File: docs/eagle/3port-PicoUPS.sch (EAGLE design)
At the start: 44 parts, among them IC1 MAX471CPA, IC2 MAX471CPA, IC3 MAX471CPA, IC6 7805TV, U1 P012PTH

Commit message: Replaced 7805 with SMD LM1117 - moved it up the board in preparation of adding switches on the output ports
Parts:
- removed IC6: 7805TV, linear:7805TV
- removed R21, R22, R23: 10k, rcl:R-TRIMM3296W
- added IC4: REG1117, burr-brown:REG1117
- added R2, R3, R7: 1k, SparkFun-Passives:RESISTOR0603-RES
- C1: value 100uF -> 10uF; device SparkFun-Capacitors:100UF-25V-20%(PTH) -> SparkFun-Capacitors:10UF-16V-10%(TANT)
- C2: device SparkFun-Capacitors:100UF-25V-20%(PTH) -> SparkFun-Capacitors:10UF-16V-10%(TANT)
- R10, R8, R9: value 1k -> 10k; device SparkFun-Passives:RESISTOR0603-RES -> rcl:R-TRIMM3296W
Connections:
- net 12V: now also IC4.VIN, R8.E; no longer IC6.VI, R21.E
- net 5V: now also IC4.VOUT; no longer IC6.VO
- net BATT-UPS: now also R9.E; no longer R22.E
- net GND: now also IC4.GND, R10.A, R2.2, R3.2, R8.A, R9.A; no longer IC6.GND, R21.A, R22.A, R23.A, R5.2, R6.2
- net I1: now also R2.1; no longer R4.1
- net I2: now also R3.1; no longer R5.1
- net I3: now also R4.1; no longer R6.1
- net N$6: now also R5.2; no longer R8.2
- net N$7: now also R6.2; no longer R9.2
- net N$8: now also R7.2; no longer R10.2
- net OUT1: now also R5.1; no longer R8.1
- net OUT2: now also R6.1; no longer R9.1
- net OUT3: now also R7.1; no longer R10.1
- net V-BATT: now also R9.S; no longer R22.S
- net V-UPS: now also R8.S; no longer R21.S
- net V-VCC: now also R10.S; no longer R23.S
- net VCC-UPS: now also R10.E; no longer R23.E
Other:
- moved on the sheet: C1, C2, R4, R5, R6

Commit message: Upgraded Eagle to 8.2.2; named 'VCC' and 'BATT' signal lines
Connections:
- net N$10 renamed BATT
- net N$9 renamed VCC
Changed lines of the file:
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@@
 <?xml version="1.0" encoding="utf-8"?>
 <!DOCTYPE eagle SYSTEM "eagle.dtd">
-<eagle version="7.6.0">
+<eagle version="8.2.2">
 <drawing>
 <settings>
@@
 </segment>
 </net>
-<net name="N$9" class="0">
+<net name="VCC" class="0">
 <segment>
 <pinref part="VCC-IN" gate="G$1" pin="P"/>
@@
 </segment>
 </net>
-<net name="N$10" class="0">
+<net name="BATT" class="0">
 <segment>
 <pinref part="BATT-IN" gate="G$1" pin="P"/>

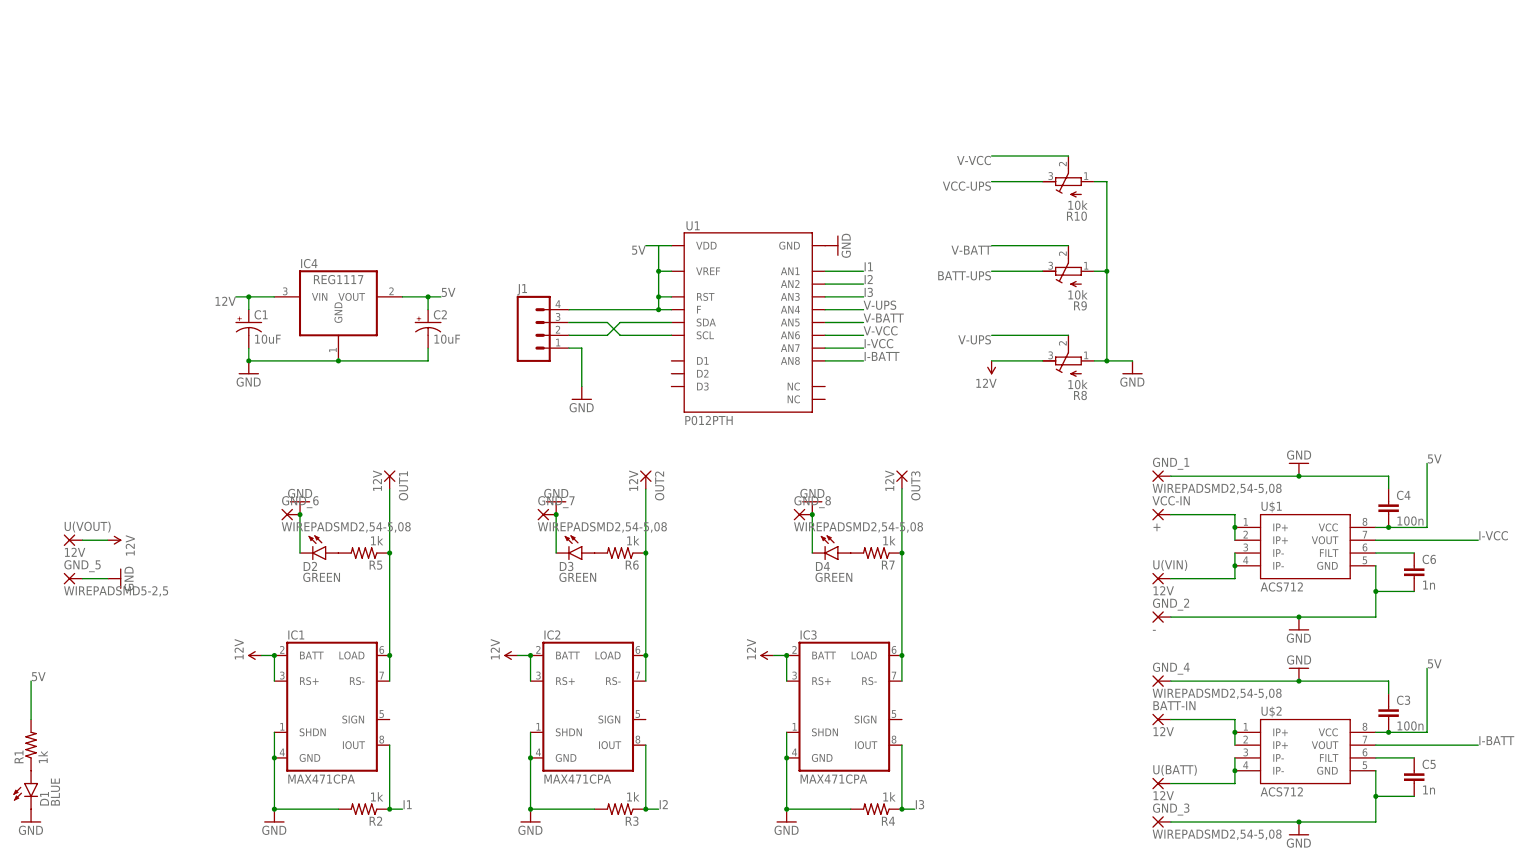
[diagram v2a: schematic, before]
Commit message: Redesign the output section to include the relays and drivers.
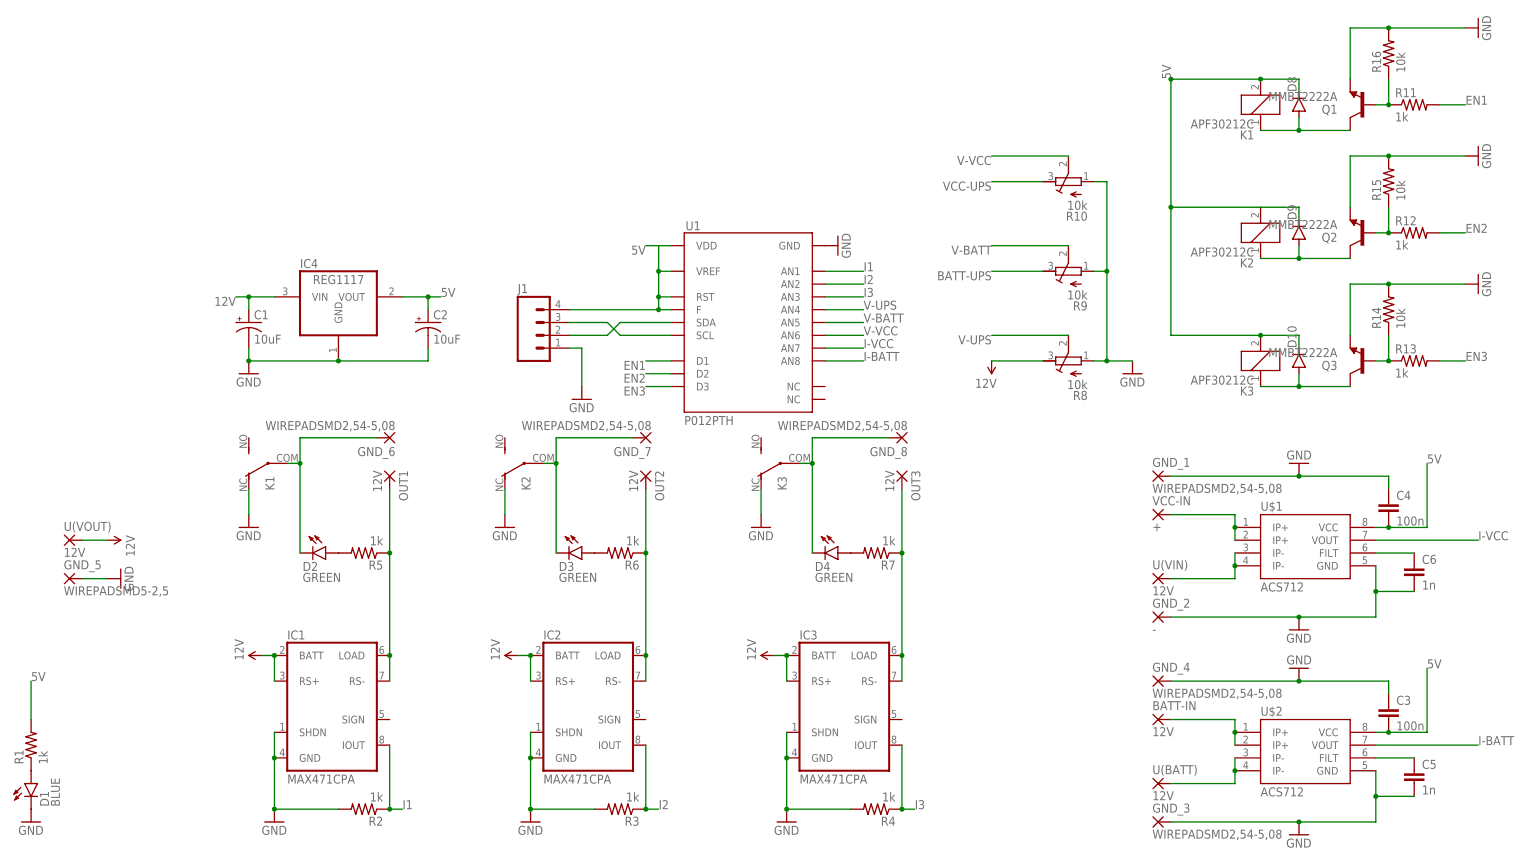
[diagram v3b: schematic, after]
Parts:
- added D10, D8, D9: (no value), SparkFun-DiscreteSemi:DIODESOD123
- added K1, K2, K3: APF30212C, relay:APF30212C
- added Q1, Q2, Q3: MMBT2222A, SparkFun-DiscreteSemi:TRANSISTOR_NPNMMBT2222A
- added R11, R12, R13: 1k, SparkFun-Passives:RESISTOR0805-RES
- added R14, R15, R16: 10k, SparkFun-Passives:RESISTOR0805-RES
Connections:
- new net EN1: R11.2, U1.D1
- new net EN2: R12.2, U1.D2
- new net EN3: R13.2, U1.D3
- new net GND_6: D2.C, GND_6.P, K12.P
- new net GND_7: D3.C, GND_7.P, K22.P
- new net GND_8: D4.C, GND_8.P, K32.P
- new net N$10: D10.A, K31.1, Q3.C
- new net N$11: Q1.B, R11.1, R16.1
- new net N$13: Q2.B, R12.1, R15.1
- new net N$14: Q3.B, R13.1, R14.1
- new net N$5: D8.A, K11.1, Q1.C
- new net N$9: D9.A, K21.1, Q2.C
- net 5V: now also D10.C, D8.C, D9.C, K11.2, K21.2, K31.2
- net GND: now also K12.O, K22.O, K32.O, Q1.E, Q2.E, Q3.E, R14.2, R15.2, R16.2; no longer D2.C, D3.C, D4.C, GND_6.P, GND_7.P, GND_8.P
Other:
- moved on the sheet: GND_6, GND_7, GND_8

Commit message: Move from 0603 to 0805 components
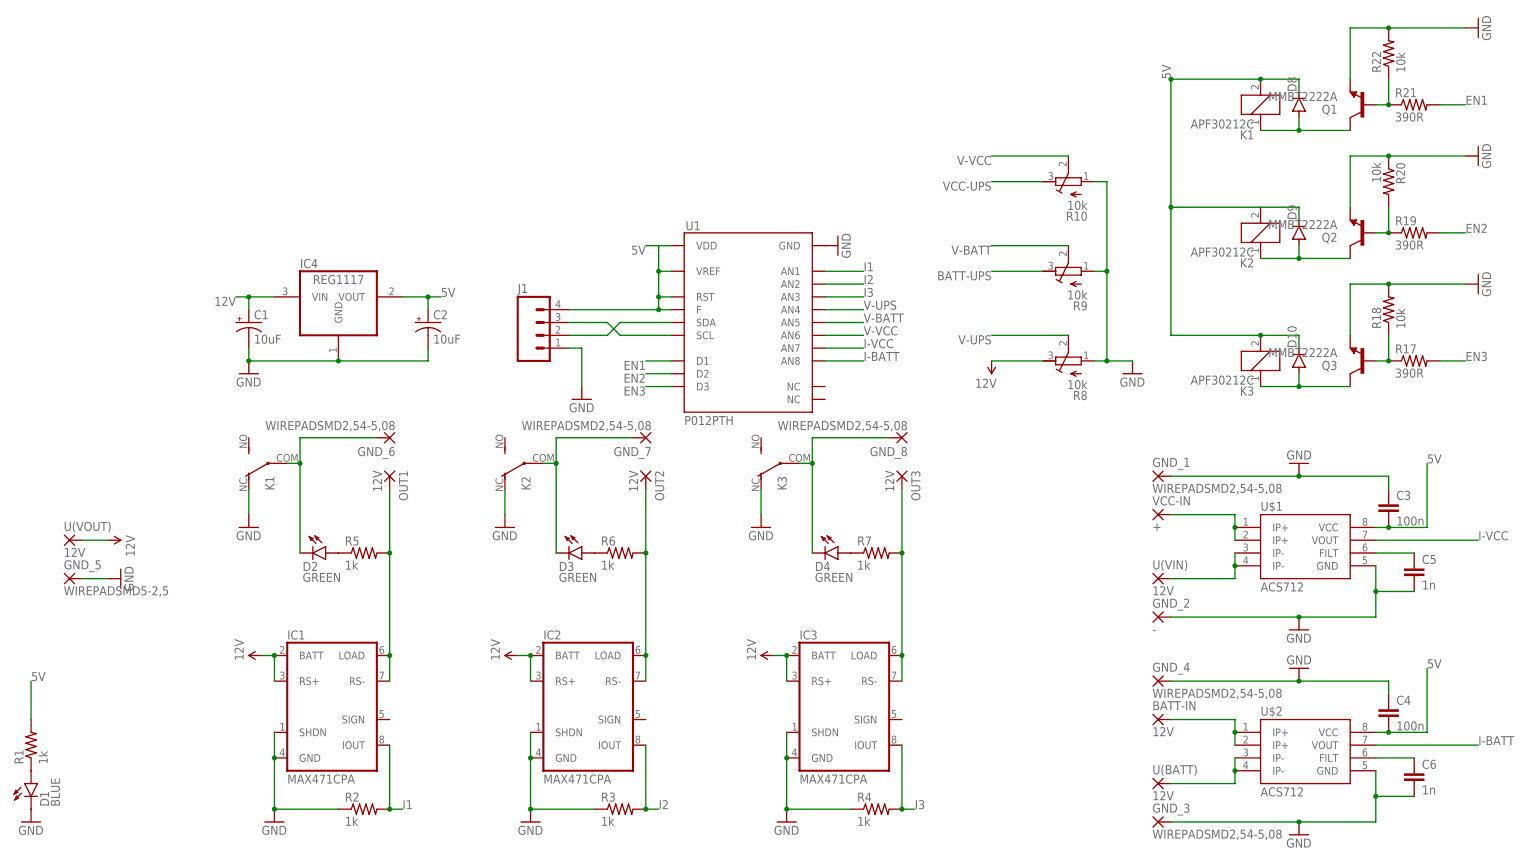
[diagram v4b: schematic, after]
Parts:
- C3, C4, C5, C6: device SparkFun-Capacitors:CAP0603-CAP -> SparkFun-Capacitors:CAP0805
- R1, R2, R3, R4, R5, R6, R7: device SparkFun-Passives:RESISTOR0603-RES -> SparkFun-Passives:RESISTOR0805-RES
- R17, R19, R21: value 1k -> 390R
- renumbered R11 to R21, R12 to R19, R13 to R17, R14 to R18, R15 to R20, R16 to R22
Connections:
- removed net N$6: D2.A, R5.2
- removed net N$7: D3.A, R6.2
- removed net N$8: D4.A, R7.2
- new net N$2: D2.A, R5.1
- new net N$3: D3.A, R6.1
- new net N$4: D4.A, R7.1
- net GND: now also R2.1, R20.1, R3.1, R4.1; no longer R2.2, R20.2, R3.2, R4.2
- net I1: now also R2.2; no longer R2.1
- net I2: now also R3.2; no longer R3.1
- net I3: now also R4.2; no longer R4.1
- net N$12: now also C5.1; no longer C6.1
- net N$13: now also R20.2; no longer R20.1
- net N$15: now also C6.1; no longer C5.1
- net OUT1: now also R5.2; no longer R5.1
- net OUT2: now also R6.2; no longer R6.1
- net OUT3: now also R7.2; no longer R7.1
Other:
- moved on the sheet: C3, C4, C5, C6, R2, R3, R4, R5, R6, R7

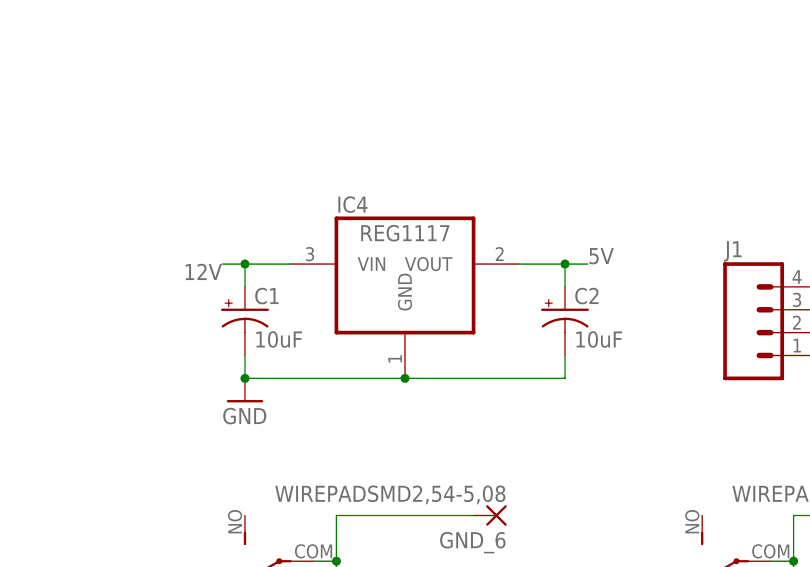
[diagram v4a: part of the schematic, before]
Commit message: Swap out AMS1117 for LM7805, as the former has max voltage of 15V, while we're running at 18V - LM7805 is rated to 20V
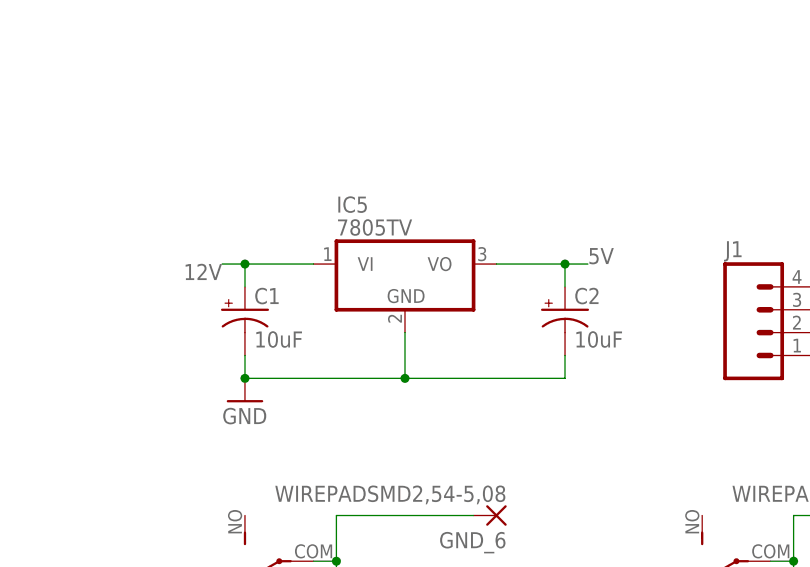
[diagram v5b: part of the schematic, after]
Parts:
- removed IC4: REG1117, burr-brown:REG1117
- added IC5: 7805TV, linear:7805TV
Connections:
- net 12V: now also IC5.VI; no longer IC4.VIN
- net 5V: now also IC5.VO; no longer IC4.VOUT
- net GND: now also IC5.GND; no longer IC4.GND
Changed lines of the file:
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@@
 <part name="J1" library="SparkFun-Connectors" deviceset="M04" device="PTH"/>
 <part name="GND16" library="SparkFun-Aesthetics" deviceset="GND" device=""/>
-<part name="IC4" library="burr-brown" deviceset="REG1117" device=""/>
 <part name="C1" library="SparkFun-Capacitors" deviceset="10UF-16V-10%(TANT)" device="" value="10uF"/>
 <part name="C2" library="SparkFun-Capacitors" deviceset="10UF-16V-10%(TANT)" device="" value="10uF"/>
@@
 <part name="C4" library="SparkFun-Capacitors" deviceset="CAP" device="0805" value="100n"/>
 <part name="C6" library="SparkFun-Capacitors" deviceset="CAP" device="0805" value="1n"/>
+<part name="IC5" library="linear" deviceset="78*" device="TV" technology="05"/>
 </parts>
 <sheets>
@@
 <instance part="J1" gate="G$1" x="106.68" y="99.06"/>
 <instance part="GND16" gate="1" x="114.3" y="86.36"/>
-<instance part="IC4" gate="G$1" x="66.04" y="106.68"/>
 <instance part="C1" gate="G$1" x="48.26" y="101.6"/>
 <instance part="C2" gate="G$1" x="83.82" y="101.6"/>
@@
 <instance part="C4" gate="G$1" x="274.32" y="22.86"/>
 <instance part="C6" gate="G$1" x="279.4" y="10.16"/>
+<instance part="IC5" gate="A1" x="66.04" y="106.68"/>
 </instances>
 <busses>
@@
 <pinref part="C1" gate="G$1" pin="+"/>
 <wire x1="48.26" y1="104.14" x2="48.26" y2="106.68" width="0.1524" layer="91"/>
-<pinref part="IC4" gate="G$1" pin="VIN"/>
-<wire x1="48.26" y1="106.68" x2="53.34" y2="106.68" width="0.1524" layer="91"/>
+<wire x1="48.26" y1="106.68" x2="55.88" y2="106.68" width="0.1524" layer="91"/>
 <wire x1="48.26" y1="106.68" x2="45.72" y2="106.68" width="0.1524" layer="91"/>
 <junction x="48.26" y="106.68"/>
 <label x="45.72" y="106.68" size="1.778" layer="95" rot="R180"/>
+<pinref part="IC5" gate="A1" pin="VI"/>
 </segment>
 </net>
@@
 <pinref part="GND12" gate="1" pin="GND"/>
 <wire x1="48.26" y1="93.98" x2="66.04" y2="93.98" width="0.1524" layer="91"/>
+<pinref part="C1" gate="G$1" pin="-"/>
 <wire x1="66.04" y1="93.98" x2="83.82" y2="93.98" width="0.1524" layer="91"/>
-<pinref part="IC4" gate="G$1" pin="GND"/>
-<junction x="66.04" y="93.98"/>
-<pinref part="C1" gate="G$1" pin="-"/>
 <wire x1="48.26" y1="93.98" x2="48.26" y2="96.52" width="0.1524" layer="91"/>
 <junction x="48.26" y="93.98"/>
 <pinref part="C2" gate="G$1" pin="-"/>
 <wire x1="83.82" y1="96.52" x2="83.82" y2="93.98" width="0.1524" layer="91"/>
+<pinref part="IC5" gate="A1" pin="GND"/>
+<wire x1="66.04" y1="99.06" x2="66.04" y2="93.98" width="0.1524" layer="91"/>
+<junction x="66.04" y="93.98"/>
 </segment>
 <segment>
@@
 </segment>
 <segment>
-<pinref part="IC4" gate="G$1" pin="VOUT"/>
 <pinref part="C2" gate="G$1" pin="+"/>
-<wire x1="78.74" y1="106.68" x2="83.82" y2="106.68" width="0.1524" layer="91"/>
+<wire x1="76.2" y1="106.68" x2="83.82" y2="106.68" width="0.1524" layer="91"/>
 <wire x1="83.82" y1="106.68" x2="83.82" y2="104.14" width="0.1524" layer="91"/>
 <wire x1="83.82" y1="106.68" x2="86.36" y2="106.68" width="0.1524" layer="91"/>
 <junction x="83.82" y="106.68"/>
 <label x="86.36" y="106.68" size="1.778" layer="95"/>
-</segment>
-<segment>
+<pinref part="IC5" gate="A1" pin="VO"/>
+</segment>
+<segment>

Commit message: Cosmetic changes - flip the direction of R20 (to be the same as R18/R22); also straighten the VBATT and VIN traces on the righthand side J4 and J6; also move the labels 'MAX471' up a bit so they are not in the solder mask
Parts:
- removed BATT-IN, OUT1, OUT2, OUT3, U(BATT), U(VIN), U(VOUT): 12V, wirepad:WIREPADSMD2,54-5,08
- removed GND_1, GND_3, GND_4, GND_6, GND_7, GND_8: WIREPADSMD2,54-5,08, wirepad:WIREPADSMD2,54-5,08
- removed GND_2: -, wirepad:WIREPADSMD2,54-5,08
- removed GND_5: WIREPADSMD5-2,5, wirepad:WIREPADSMD5-2,5
- removed VCC-IN: +, wirepad:WIREPADSMD2,54-5,08
- added J2, J3, J4, J5, J6, J7, J8, J9: (no value), SparkFun-Connectors:M025MM
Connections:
- net 12V: now also J2.2; no longer U(VOUT).P
- net BATT: now also J5.1; no longer BATT-IN.P
- net BATT-UPS: now also J6.2; no longer U(BATT).P
- net GND: now also J2.1, J3.2, J4.1, J5.2, J6.1, R20.2; no longer GND_1.P, GND_2.P, GND_3.P, GND_4.P, GND_5.P, R20.1
- net GND_6: now also J9.1; no longer GND_6.P
- net GND_7: now also J8.1; no longer GND_7.P
- net GND_8: now also J7.1; no longer GND_8.P
- net N$13: now also R20.1; no longer R20.2
- net OUT1: now also J9.2; no longer OUT1.P
- net OUT2: now also J8.2; no longer OUT2.P
- net OUT3: now also J7.2; no longer OUT3.P
- net VCC: now also J3.1; no longer VCC-IN.P
- net VCC-UPS: now also J4.2; no longer U(VIN).P
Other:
- moved on the sheet: R20
